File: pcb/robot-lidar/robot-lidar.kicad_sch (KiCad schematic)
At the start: 38 parts, among them J10 Conn_01x18, J11 USB_A, J12 Conn_02x20_Odd_Even, J2 YLIDAR X4, J3 Jack-DC, J5 Conn_01x02, J5 Conn_02x03_Odd_Even, J6 Conn_01x02, J7 Conn_01x02, J7 Conn_ARM_SWD_TagConnect_TC2030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

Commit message: saving shematic
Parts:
- removed J10, J9: Conn_01x18, Connector_PinHeader_2.54mm:PinHeader_1x18_P2.54mm_Vertical, symbol Connector_Generic:Conn_01x18
- J12: footprint (none) -> Connector_PinHeader_2.54mm:PinHeader_2x20_P2.54mm_Vertical
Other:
- moved on the sheet: J12

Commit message: finish V2
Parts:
- removed J11: USB_A, Connector_USB:USB_A_Molex_48037-2200_Horizontal, symbol Connector:USB_A
- removed R13, R14: 10K, Resistor_SMD:R_0603_1608Metric, symbol Device:R
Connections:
- net I2C_SCL is gone; now on net SCL: R1.2, U2.23 (SCL)
- net I2C_SDA is gone; now on net SDA: R2.2, U2.24 (SDA)
- net INT is gone; now on net MOTOR_2_B: U1.18 (PB0)
- net UART4_RX is gone; now on net UART_RX: J2.2 (Pin_2)
- net UART4_TX is gone; now on net UART_TX: J2.3 (Pin_3)
- net DEV_EN: now also J12.29 (Pin_29)
- net MOTOR_1_A: now also U1.16 (PA6); no longer U1.12 (PA2)
- net MOTOR_1_B: now also U1.17 (PA7); no longer U1.13 (PA3)
- net MOTOR_2_A: now also U1.19 (PB1); no longer U1.10 (PA0)
- net MOTOR_2_B: no longer U1.11 (PA1)
- net MOTOR_3_A: now also U1.42 (PB6); no longer U1.16 (PA6)
- net MOTOR_3_B: now also U1.43 (PB7); no longer U1.17 (PA7)
- net MOTOR_4_A: now also U1.45 (PB8); no longer U1.29 (PA8)
- net MOTOR_4_B: now also U1.46 (PB9); no longer U1.30 (PA9)
- net M_EN: now also J12.31 (Pin_31)
- net M_SCTR: now also J12.32 (Pin_32)
- net SCL: now also J12.5 (Pin_5)
- net SDA: now also J12.3 (Pin_3)

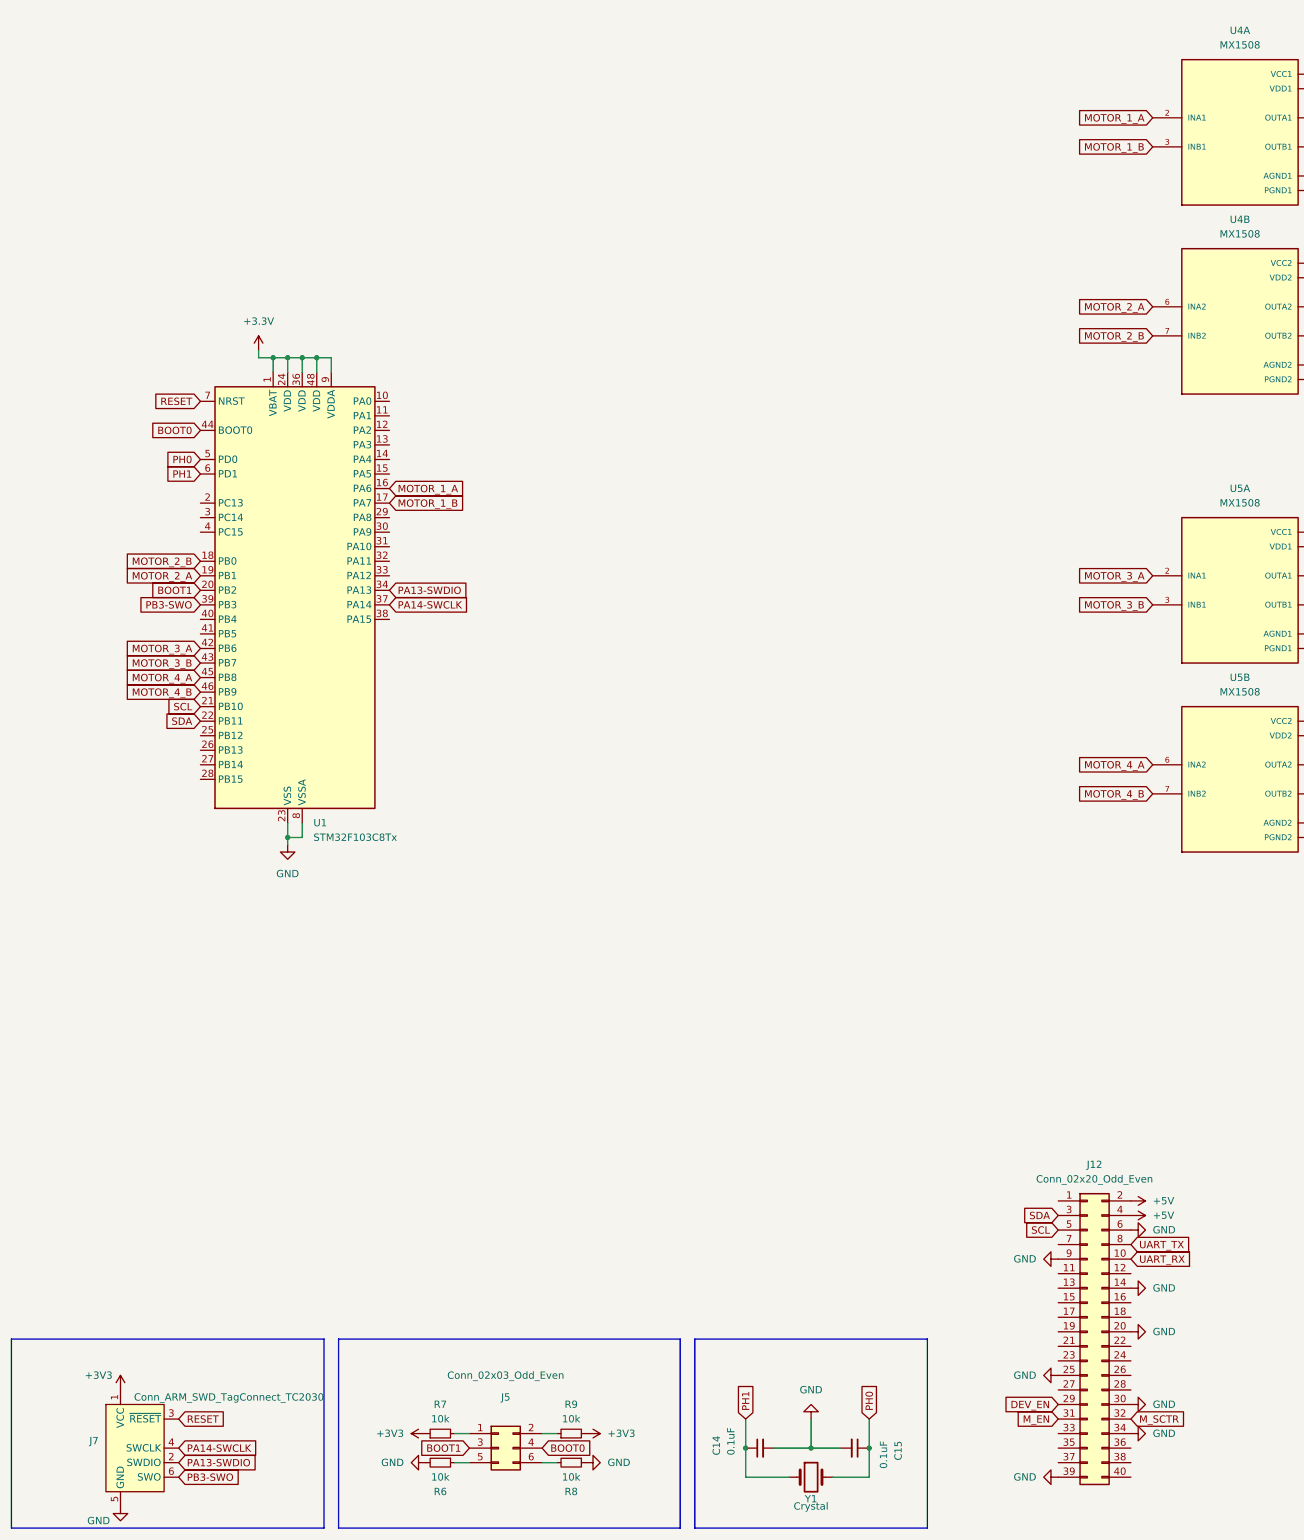
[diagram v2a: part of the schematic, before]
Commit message: rewire i2c
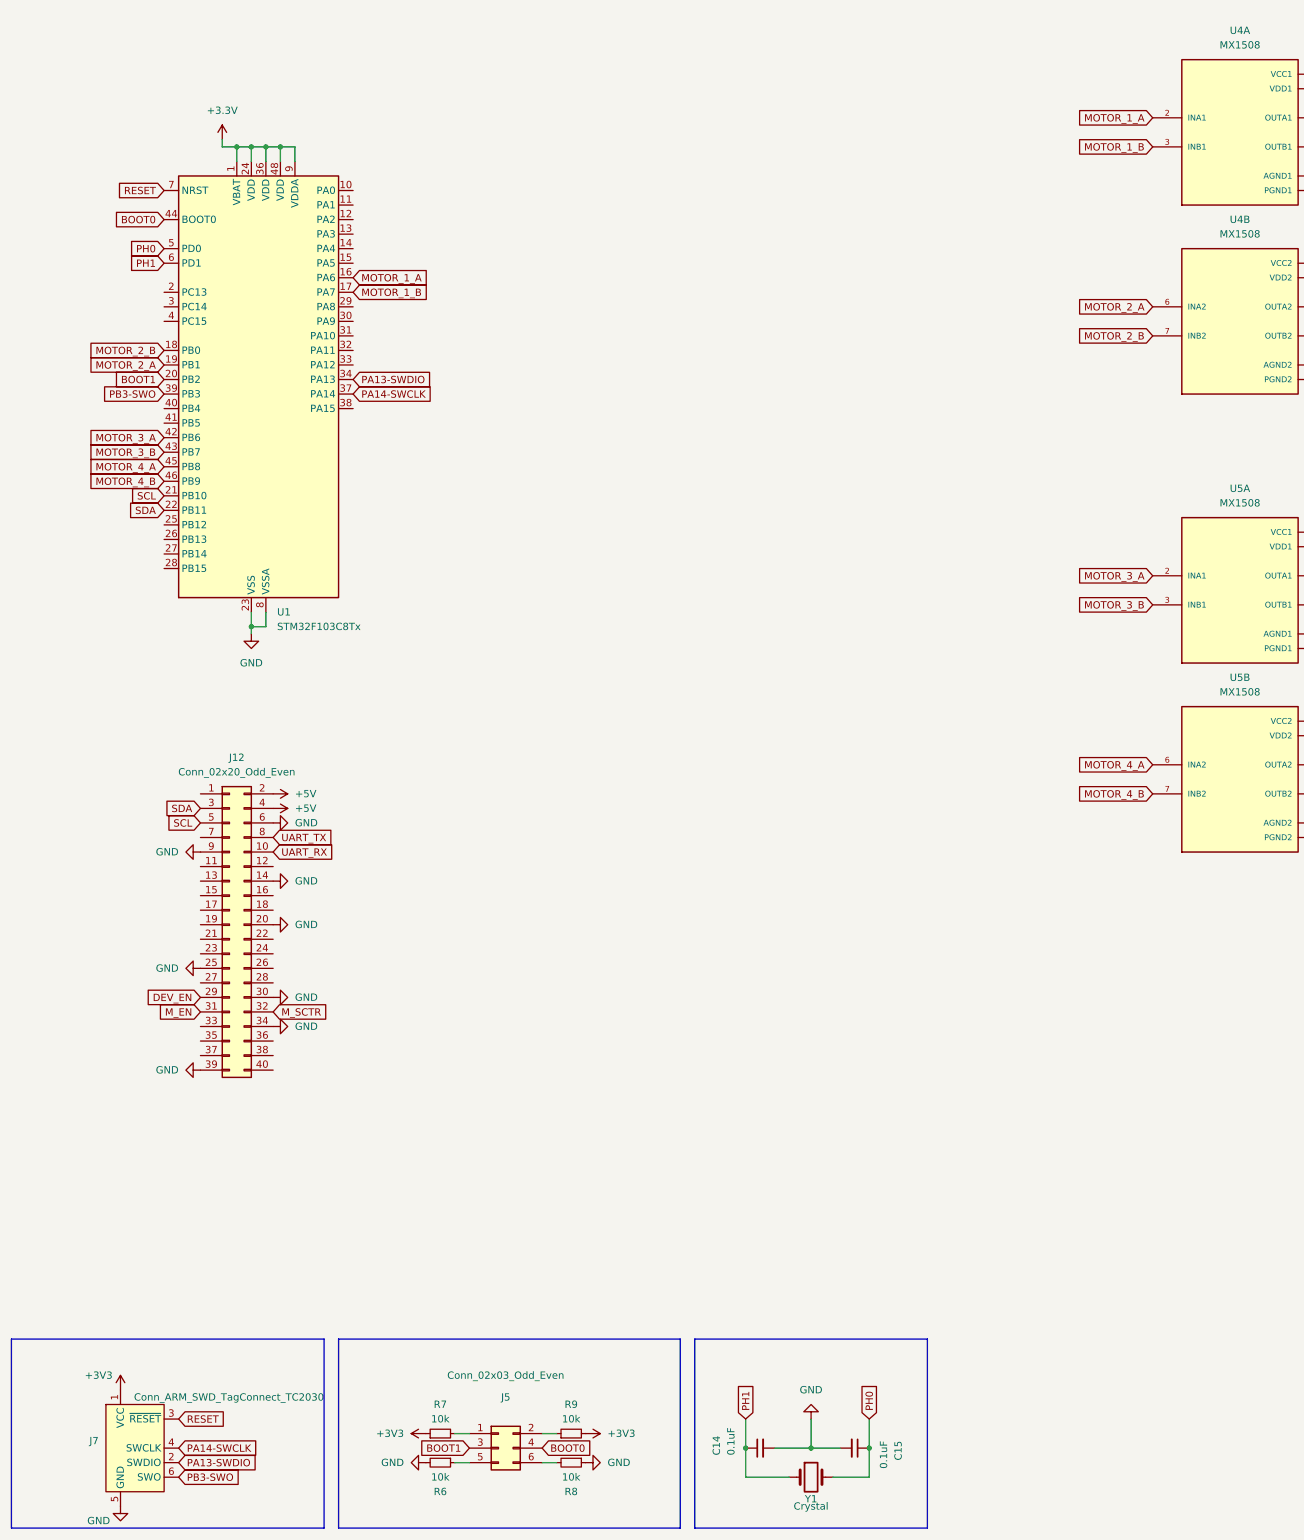
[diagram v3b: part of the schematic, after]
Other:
- moved on the sheet: J12, U1

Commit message: PCA9685
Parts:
- removed C14, C15: 0.1uF, Capacitor_SMD:C_0603_1608Metric, symbol Device:C_Small
- removed J5: Conn_02x03_Odd_Even, Connector_PinHeader_2.54mm:PinHeader_2x03_P2.54mm_Vertical_SMD, symbol Connector_Generic:Conn_02x03_Odd_Even
- removed J7: Conn_ARM_SWD_TagConnect_TC2030, Connector_PinHeader_2.54mm:PinHeader_1x06_P2.54mm_Vertical, symbol Connector:Conn_ARM_SWD_TagConnect_TC2030
- removed R6, R7, R8, R9: 10k, Resistor_SMD:R_0603_1608Metric, symbol Device:R_Small
- removed U1: STM32F103C8Tx, Package_QFP:LQFP-48_7x7mm_P0.5mm, symbol MCU_ST_STM32F1:STM32F103C8Tx
- removed Y1: Crystal, Crystal:Crystal_SMD_HC49-SD, symbol Device:Crystal
- added R1: R_Small, Resistor_SMD:R_0603_1608Metric, symbol Device:R_Small
- added U1: PCA9635, Package_SO:TSSOP-28_4.4x9.7mm_P0.65mm, symbol Driver_LED:PCA9635
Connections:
- net +5V: now also U1.28 (VDD)
- net GND: now also R1.1, U1.1 (A0), U1.14 (VSS), U1.2 (A1), U1.24 (A5), U1.25 (A6), U1.3 (A2), U1.4 (A3), U1.5 (A4)
- net MOTOR_1_A: now also U1.6 (LED0)
- net MOTOR_1_B: now also U1.7 (LED1)
- net MOTOR_2_A: now also U1.8 (LED2)
- net MOTOR_2_B: now also U1.9 (LED3)
- net MOTOR_3_A: now also U1.10 (LED4)
- net MOTOR_3_B: now also U1.11 (LED5)
- net MOTOR_4_A: now also U1.12 (LED6)
- net MOTOR_4_B: now also U1.13 (LED7)
- net SCL: now also U1.26 (SCL)
- net SDA: now also U1.27 (SDA)
- new net: R1.2, U1.23 (~{OE})
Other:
- moved on the sheet: C1, C2, C3, R1, R2, U2

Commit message: wiring pca
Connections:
- net MOTOR_1_A: now also U1.9 (LED3); no longer U1.6 (LED0)
- net MOTOR_1_B: now also U1.8 (LED2); no longer U1.7 (LED1)
- net MOTOR_2_A: now also U1.6 (LED0); no longer U1.8 (LED2)
- net MOTOR_2_B: now also U1.7 (LED1); no longer U1.9 (LED3)
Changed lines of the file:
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@@
+    )
+  )
+  (global_label "MOTOR_2_A" (shape input) (at 115.57 54.61 0) (fields_autoplaced)
+    (effects (font (size 1.27 1.27)) (justify left))
+    (property "Intersheetrefs" "${INTERSHEET_REFS}" (at 129.0591 54.61 0)
+      (effects (font (size 1.27 1.27)) (justify left) hide)
     )
   )
@@
     )
   )
+  (global_label "MOTOR_1_A" (shape input) (at 115.57 62.23 0) (fields_autoplaced)
+    (effects (font (size 1.27 1.27)) (justify left))
+    (property "Intersheetrefs" "${INTERSHEET_REFS}" (at 129.0591 62.23 0)
+      (effects (font (size 1.27 1.27)) (justify left) hide)
+    )
+  )
   (global_label "M_EN" (shape input) (at 48.26 190.5 180) (fields_autoplaced)
     (effects (font (size 1.27 1.27)) (justify right))
@@
     )
   )
-  (global_label "MOTOR_1_A" (shape input) (at 115.57 54.61 0) (fields_autoplaced)
-    (effects (font (size 1.27 1.27)) (justify left))
-    (property "Intersheetrefs" "${INTERSHEET_REFS}" (at 129.0591 54.61 0)
-      (effects (font (size 1.27 1.27)) (justify left) hide)
-    )
-  )
   (global_label "MOTOR_4_A" (shape input) (at 214.63 147.32 180) (fields_autoplaced)
     (effects (font (size 1.27 1.27)) (justify right))
@@
     )
   )
-  (global_label "MOTOR_1_B" (shape input) (at 115.57 57.15 0) (fields_autoplaced)
+  (global_label "MOTOR_2_B" (shape input) (at 115.57 57.15 0) (fields_autoplaced)
     (effects (font (size 1.27 1.27)) (justify left))
     (property "Intersheetrefs" "${INTERSHEET_REFS}" (at 129.2405 57.15 0)
@@
     )
   )
-  (global_label "MOTOR_2_A" (shape input) (at 115.57 59.69 0) (fields_autoplaced)
+  (global_label "MOTOR_1_B" (shape input) (at 115.57 59.69 0) (fields_autoplaced)
     (effects (font (size 1.27 1.27)) (justify left))
-    (property "Intersheetrefs" "${INTERSHEET_REFS}" (at 129.0591 59.69 0)
+    (property "Intersheetrefs" "${INTERSHEET_REFS}" (at 129.2405 59.69 0)
       (effects (font (size 1.27 1.27)) (justify left) hide)
     )
@@
     )
   )
-  (global_label "MOTOR_2_B" (shape input) (at 115.57 62.23 0) (fields_autoplaced)
-    (effects (font (size 1.27 1.27)) (justify left))
-    (property "Intersheetrefs" "${INTERSHEET_REFS}" (at 129.2405 62.23 0)
-      (effects (font (size 1.27 1.27)) (justify left) hide)
-    )
-  )

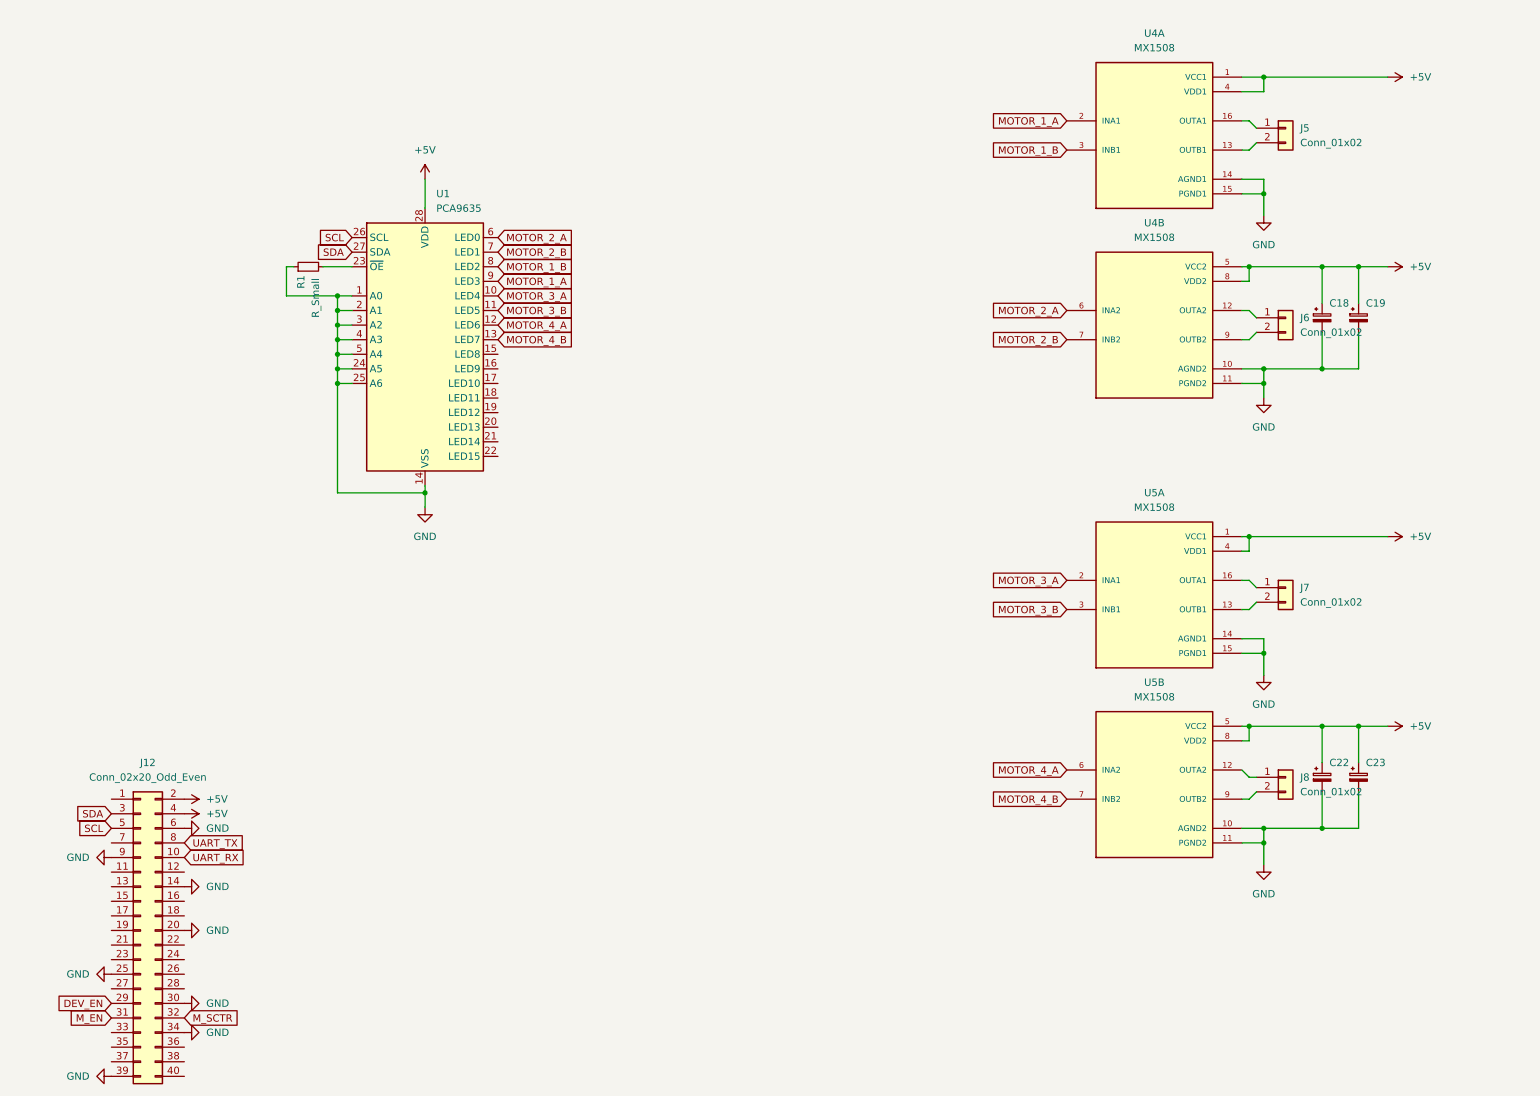
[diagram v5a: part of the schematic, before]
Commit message: remove two motor control and change i2c motor by atmgea328p
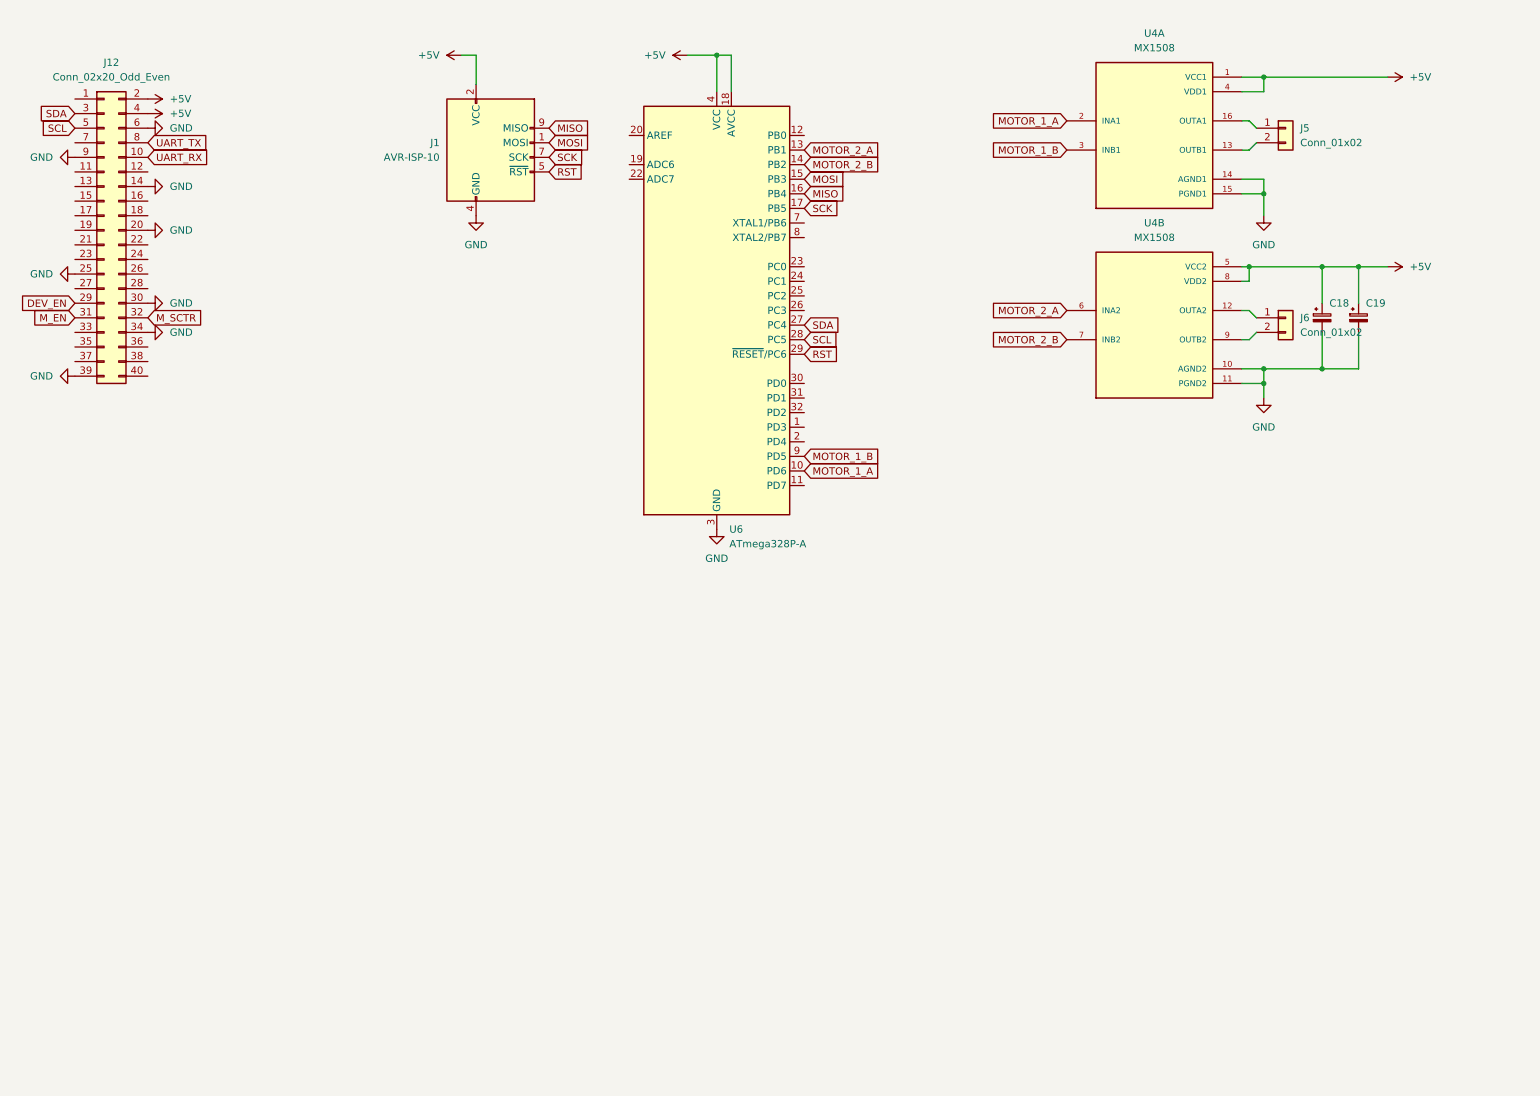
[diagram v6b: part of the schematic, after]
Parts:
- removed C22, C23: C_Polarized_Small, Capacitor_SMD:CP_Elec_6.3x4.9, symbol Device:C_Polarized_Small
- removed J7, J8: Conn_01x02, Connector_PinSocket_2.54mm:PinSocket_1x02_P2.54mm_Vertical, symbol Connector_Generic:Conn_01x02
- removed R1: R_Small, Resistor_SMD:R_0603_1608Metric, symbol Device:R_Small
- removed U1: PCA9635, Package_SO:TSSOP-28_4.4x9.7mm_P0.65mm, symbol Driver_LED:PCA9635
- removed U5: MX1508, MX1508:SOIC127P600X177-16N, symbol MX1508:MX1508
- added J1: AVR-ISP-10, symbol Connector:AVR-ISP-10
- added U6: ATmega328P-A, Package_QFP:TQFP-32_7x7mm_P0.8mm, symbol MCU_Microchip_ATmega:ATmega328P-A
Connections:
- net +5V: now also J1.2 (VCC), U6.18 (AVCC), U6.4 (VCC), U6.6 (VCC)
- net GND: now also J1.10 (GND), J1.4 (GND), J1.6 (GND), J1.8 (GND), U6.21 (GND), U6.3 (GND), U6.5 (GND)
- net MOTOR_1_A: now also U6.10 (PD6)
- net MOTOR_1_B: now also U6.9 (PD5)
- net MOTOR_2_A: now also U6.13 (PB1)
- net MOTOR_2_B: now also U6.14 (PB2)
- net SCL: now also U6.28 (PC5)
- net SDA: now also U6.27 (PC4)
- new net MISO: J1.9 (MISO), U6.16 (PB4)
- new net MOSI: J1.1 (MOSI), U6.15 (PB3)
- new net RST: J1.5 (~{RST}), U6.29 (~{RESET}/PC6)
- new net SCK: J1.7 (SCK), U6.17 (PB5)
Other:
- moved on the sheet: J12
